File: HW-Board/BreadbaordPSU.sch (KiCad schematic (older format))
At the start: 42 parts, among them J1 vin, J2 Outputs, Q1 Si4435, U1 MAX6241, U11 LM2937, U12 ROE-0505S, U13 FAN5331, U7 SPX3819M5-L-3-3

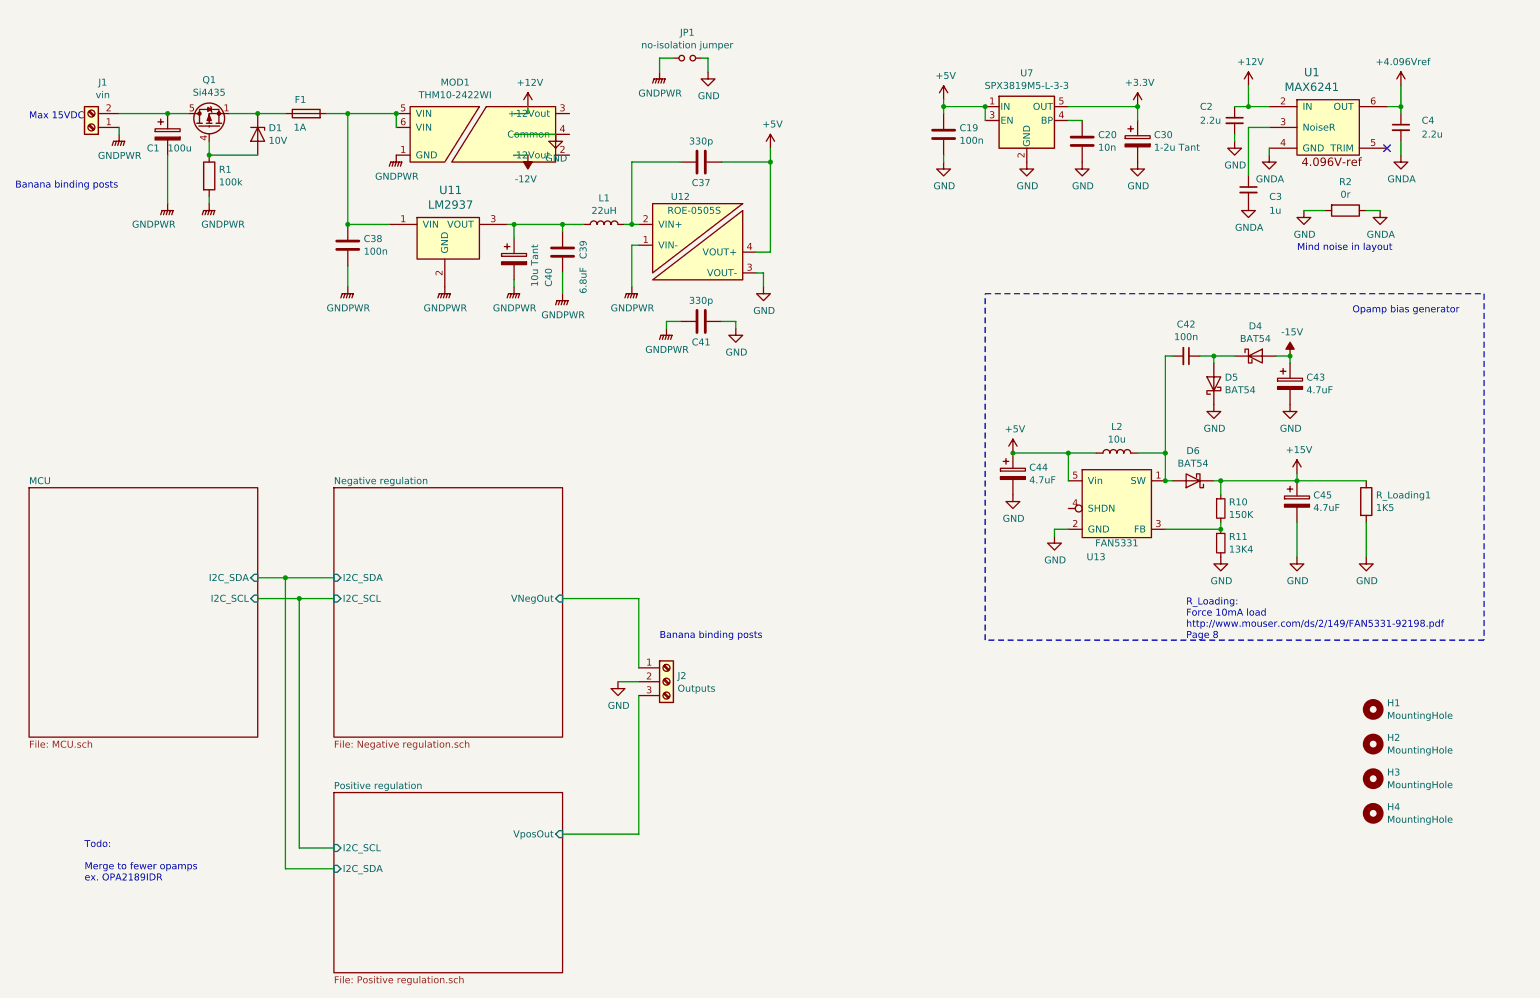
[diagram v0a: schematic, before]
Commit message: pre-regulator for 5 v rail
Takes Vin max to above 24V
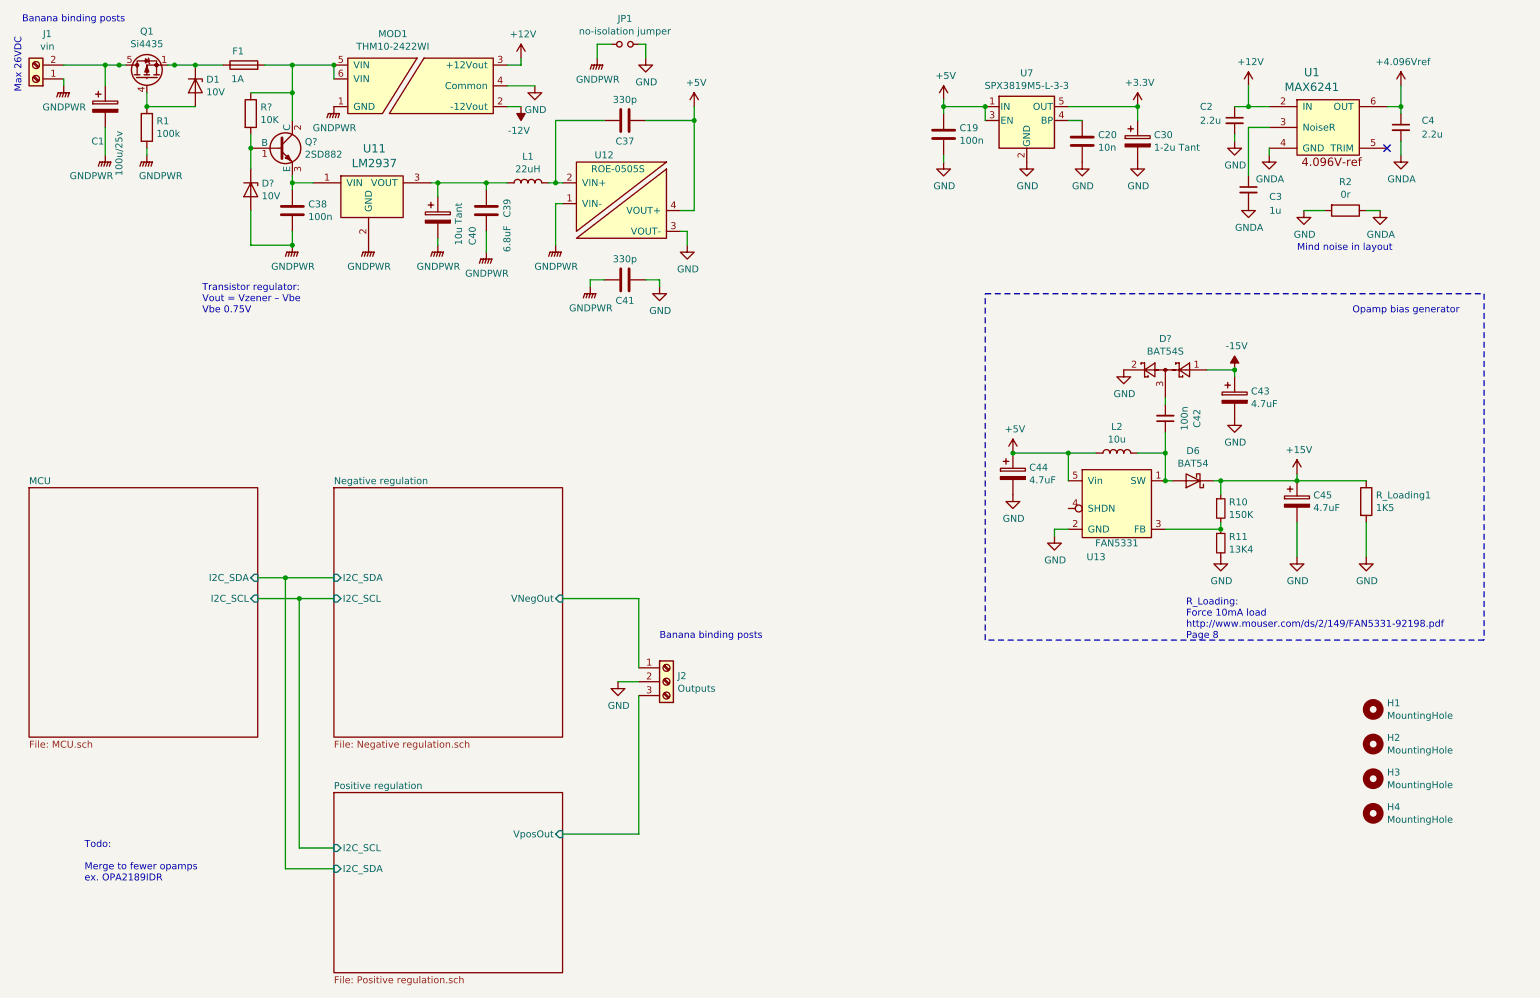
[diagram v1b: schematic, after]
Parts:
- removed D4, D5: BAT54, symbol Device:D_Schottky
- added D?: 10V, symbol Device:D_Zener
- added D?: BAT54S, Package_TO_SOT_SMD:SOT-23, symbol Diode:BAT54S
- added Q?: 2SD882, Package_TO_SOT_THT:TO-126-3_Vertical, symbol Peters:2SD882
- added R?: 10K, Resistor_SMD:R_0805_2012Metric_Pad1.15x1.40mm_HandSolder, symbol Device:R
- C1: value 100u -> 100u/25v
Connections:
- net +12V: now also MOD1.3 (+12Vout)
- net -12V: now also MOD1.2 (-12Vout)
- net -15V: now also D?.1
- net GND: now also MOD1.4 (Common), D?.2
- net GNDPWR: now also D?.2 (A)
- net at F1.2, MOD1.5 (VIN), MOD1.6 (VIN): now also Q?.2 (C), R?.1; no longer C38.1, U11.1 (VIN)
- net at D1.1 (K), F1.1, Q1.1 (S): now also Q1.2 (S), Q1.3 (S)
- net at C1.1, J1.2 (Pin_2), Q1.5 (D): now also Q1.6 (D), Q1.7 (D), Q1.8 (D)
- net at D6.2 (A), L2.2, U13.1 (SW): now also C42.1; no longer C42.2
- new net: C38.1, Q?.3 (E), U11.1 (VIN)
- new net: C42.2, D?.3
- new net: D?.1 (K), Q?.1 (B), R?.2
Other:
- note added: "Max 26VDC"
- note added: "Transistor regulator:\nVout = Vzener – Vbe\nVbe 0.75V"
- note removed: "Max 15VDC"
- moved on the sheet: C1, C37, C38, C39, C40, C41, C42, C43, D1, F1, J1, JP1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

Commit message: PDF sync
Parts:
- C40: footprint (none) -> Capacitor_Tantalum_SMD:CP_EIA-3528-12_Kemet-T_Pad1.50x2.35mm_HandSolder
- D1: footprint (none) -> Diode_THT:D_DO-35_SOD27_P7.62mm_Horizontal
- D4: renamed from D?; footprint (none) -> Diode_THT:D_DO-35_SOD27_P7.62mm_Horizontal
- D6: footprint (none) -> Package_TO_SOT_SMD:SOT-23
- H1, H2, H3, H4: footprint (none) -> MountingHole:MountingHole_3.2mm_M3_DIN965
- JP1: footprint (none) -> Connector_PinSocket_2.54mm:PinSocket_1x02_P2.54mm_Vertical
- U12: footprint (none) -> Libs:ROE-0505S
- gave numbers to parts that had none: 3
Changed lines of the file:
@@
 F 0 "JP1" H 4950 935 50  0000 C CNN
 F 1 "no-isolation jumper" H 4950 844 50  0000 C CNN
-F 2 "" H 4950 750 50  0001 C CNN
+F 2 "Connector_PinSocket_2.54mm:PinSocket_1x02_P2.54mm_Vertical" H 4950 750 50  0001 C CNN
 F 3 "~" H 4950 750 50  0001 C CNN
 	1    4950 750
@@
 F 0 "D1" V 1804 1129 50  0000 L CNN
 F 1 "10V" V 1895 1129 50  0000 L CNN
-F 2 "" H 1850 1050 50  0001 C CNN
+F 2 "Diode_THT:D_DO-35_SOD27_P7.62mm_Horizontal" H 1850 1050 50  0001 C CNN
 F 3 "~" H 1850 1050 50  0001 C CNN
 	1    1850 1050
@@
 F 0 "H1" H 10450 5596 50  0000 L CNN
 F 1 "MountingHole" H 10450 5505 50  0000 L CNN
-F 2 "" H 10350 5550 50  0001 C CNN
+F 2 "MountingHole:MountingHole_3.2mm_M3_DIN965" H 10350 5550 50  0001 C CNN
 F 3 "~" H 10350 5550 50  0001 C CNN
 	1    10350 5550
@@
 F 0 "H2" H 10450 5846 50  0000 L CNN
 F 1 "MountingHole" H 10450 5755 50  0000 L CNN
-F 2 "" H 10350 5800 50  0001 C CNN
+F 2 "MountingHole:MountingHole_3.2mm_M3_DIN965" H 10350 5800 50  0001 C CNN
 F 3 "~" H 10350 5800 50  0001 C CNN
 	1    10350 5800
@@
 F 0 "H3" H 10450 6096 50  0000 L CNN
 F 1 "MountingHole" H 10450 6005 50  0000 L CNN
-F 2 "" H 10350 6050 50  0001 C CNN
+F 2 "MountingHole:MountingHole_3.2mm_M3_DIN965" H 10350 6050 50  0001 C CNN
 F 3 "~" H 10350 6050 50  0001 C CNN
 	1    10350 6050
@@
 F 0 "H4" H 10450 6346 50  0000 L CNN
 F 1 "MountingHole" H 10450 6255 50  0000 L CNN
-F 2 "" H 10350 6300 50  0001 C CNN
+F 2 "MountingHole:MountingHole_3.2mm_M3_DIN965" H 10350 6300 50  0001 C CNN
 F 3 "~" H 10350 6300 50  0001 C CNN
 	1    10350 6300
@@
 F 0 "D6" H 9050 3684 50  0000 C CNN
 F 1 "BAT54" H 9050 3775 50  0000 C CNN
-F 2 "" H 9050 3900 50  0001 C CNN
+F 2 "Package_TO_SOT_SMD:SOT-23" H 9050 3900 50  0001 C CNN
 F 3 "~" H 9050 3900 50  0001 C CNN
 	1    9050 3900
@@
 	2550 900  2850 900
 $Comp
-L Device:R R?
+L Device:R R14
 U 1 1 5D75C87F
 P 2250 1250
-F 0 "R?" H 2320 1296 50  0000 L CNN
+F 0 "R14" H 2320 1296 50  0000 L CNN
 F 1 "10K" H 2320 1205 50  0000 L CNN
 F 2 "Resistor_SMD:R_0805_2012Metric_Pad1.15x1.40mm_HandSolder" V 2180 1250 50  0001 C CNN
@@
 $EndComp
 $Comp
-L Device:D_Zener D?
+L Device:D_Zener D4
 U 1 1 5D75CF0B
 P 2250 1800
-F 0 "D?" V 2204 1879 50  0000 L CNN
+F 0 "D4" V 2204 1879 50  0000 L CNN
 F 1 "10V" V 2295 1879 50  0000 L CNN
-F 2 "" H 2250 1800 50  0001 C CNN
+F 2 "Diode_THT:D_DO-35_SOD27_P7.62mm_Horizontal" H 2250 1800 50  0001 C CNN
 F 3 "~" H 2250 1800 50  0001 C CNN
 	1    2250 1800
@@
 F 0 "C40" V 3850 1800 50  0000 L CNN
 F 1 "10u Tant" V 3750 1800 50  0000 L CNN
-F 2 "" H 3638 1850 50  0001 C CNN
+F 2 "Capacitor_Tantalum_SMD:CP_EIA-3528-12_Kemet-T_Pad1.50x2.35mm_HandSolder" H 3638 1850 50  0001 C CNN
 F 3 "~" H 3600 2000 50  0001 C CNN
 	1    3600 2000
@@
 F 0 "U12" H 4800 2150 50  0000 C CNN
 F 1 "ROE-0505S" H 4900 2050 50  0000 C CNN
-F 2 "" H 5350 2450 50  0001 C CNN
+F 2 "Libs:ROE-0505S" H 5350 2450 50  0001 C CNN
 F 3 "http://192.168.0.102/api/part_attachments/1968/getFile" H 5400 2200 50  0001 C CNN
 	1    4950 1850
@@
 Transistor regulator:\nVout = Vzener – Vbe\nVbe 0.75V
 $Comp
-L Peters:2SD882 Q?
+L Peters:2SD882 Q4
 U 1 1 5D7AEDF2
 P 2450 1500
-F 0 "Q?" H 2640 1546 50  0000 L CNN
+F 0 "Q4" H 2640 1546 50  0000 L CNN
 F 1 "2SD882" H 2640 1455 50  0000 L CNN
 F 2 "Package_TO_SOT_THT:TO-126-3_Vertical" H 2650 1425 50  0001 L CIN
@@
 	2250 1500 2250 1650
 $Comp
-L Diode:BAT54S D?
+L Diode:BAT54S D5
 U 1 1 5D7B9F8B
 P 8850 3100
-F 0 "D?" H 8850 3325 50  0000 C CNN
+F 0 "D5" H 8850 3325 50  0000 C CNN
 F 1 "BAT54S" H 8850 3234 50  0000 C CNN
 F 2 "Package_TO_SOT_SMD:SOT-23" H 8925 3225 50  0001 L CNN
